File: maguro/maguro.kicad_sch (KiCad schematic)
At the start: 1 part

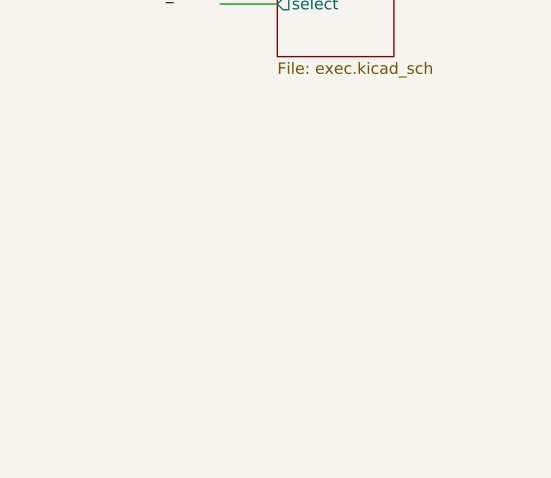
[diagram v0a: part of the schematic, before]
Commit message: Added joysticks
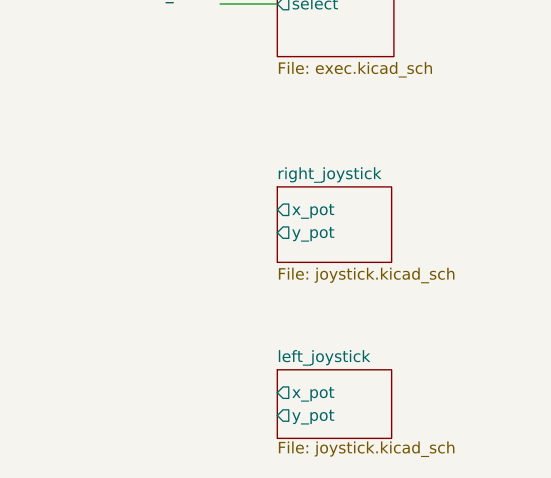
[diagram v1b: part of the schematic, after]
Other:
- added sheet left_joystick (joystick.kicad_sch)
- added sheet right_joystick (joystick.kicad_sch)
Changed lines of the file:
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@@
+		)
+	)
+	(sheet
+		(at 203.2 127)
+		(size 12.7 8.382)
+		(exclude_from_sim no)
+		(in_bom yes)
+		(on_board yes)
+		(dnp no)
+		(fields_autoplaced yes)
+		(stroke
+			(width 0.1524)
+			(type solid)
+		)
+		(fill
+			(color 0 0 0 0.0000)
+		)
+		(property "Sheetname" "right_joystick"
+			(at 203.2 126.2884 0)
+			(effects
+				(font
+					(size 1.27 1.27)
+				)
+				(justify left bottom)
+			)
+		)
+		(property "Sheetfile" "joystick.kicad_sch"
+			(at 203.2 135.9666 0)
+			(effects
+				(font
+					(size 1.27 1.27)
+				)
+				(justify left top)
+			)
+		)
+		(pin "x_pot" output
+			(at 203.2 129.54 180)
+			(effects
+				(font
+					(size 1.27 1.27)
+				)
+				(justify left)
+			)
+		)
+		(pin "y_pot" output
+			(at 203.2 132.08 180)
+			(effects
+				(font
+					(size 1.27 1.27)
+				)
+				(justify left)
+			)
+		)
+		(instances
+			(project "maguro"
+				(path "/64a35719-70ce-4bea-be36-7f0da599755f"
+					(page "16")
+				)
+			)
+		)
+	)
+	(sheet
+		(at 203.2 147.32)
+		(size 12.7 7.62)
+		(exclude_from_sim no)
+		(in_bom yes)
+		(on_board yes)
+		(dnp no)
+		(fields_autoplaced yes)
+		(stroke
+			(width 0.1524)
+			(type solid)
+		)
+		(fill
+			(color 0 0 0 0.0000)
+		)
+		(property "Sheetname" "left_joystick"
+			(at 203.2 146.6084 0)
+			(effects
+				(font
+					(size 1.27 1.27)
+				)
+				(justify left bottom)
+			)
+		)
+		(property "Sheetfile" "joystick.kicad_sch"
+			(at 203.2 155.2706 0)
+			(effects
+				(font
+					(size 1.27 1.27)
+				)
+				(justify left top)
+			)
+		)
+		(property "Field2" ""
+			(at 203.2 147.32 0)
+			(effects
+				(font
+					(size 1.27 1.27)
+				)
+			)
+		)
+		(pin "x_pot" output
+			(at 203.2 149.86 180)
+			(effects
+				(font
+					(size 1.27 1.27)
+				)
+				(justify left)
+			)
+		)
+		(pin "y_pot" output
+			(at 203.2 152.4 180)
+			(effects
+				(font
+					(size 1.27 1.27)
+				)
+				(justify left)
+			)
+		)
+		(instances
+			(project "maguro"
+				(path "/64a35719-70ce-4bea-be36-7f0da599755f"
+					(page "15")
+				)
+			)
 		)
 	)

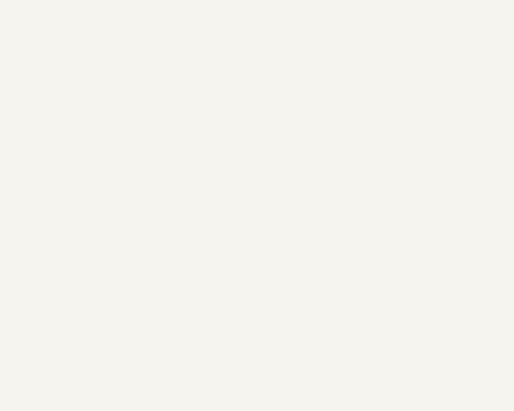
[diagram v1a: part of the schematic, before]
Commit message: Added silkscreen
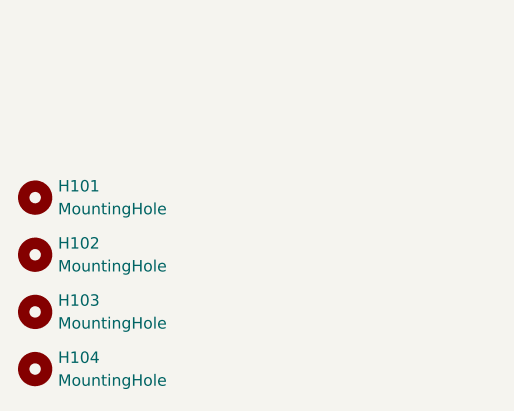
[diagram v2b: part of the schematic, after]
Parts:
- added H101, H102, H103, H104: MountingHole, MountingHole:MountingHole_2.7mm_M2.5, symbol Mechanical:MountingHole
